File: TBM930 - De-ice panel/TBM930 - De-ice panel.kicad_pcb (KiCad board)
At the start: 2 copper layers, 190.5 x 101.6 mm, 23 parts, among them Q1 BS170, Q2 BS170, Q3 BS170, SW1 SW_SPDT, SW2 SW_SPDT, SW3 SW_SPDT, SW4 SW_SPDT, SW5 SW_SPDT, SW6 SW_SPDT, SW7 SW_SPDT, U1 ArduinoMEGA2560PROEmbed

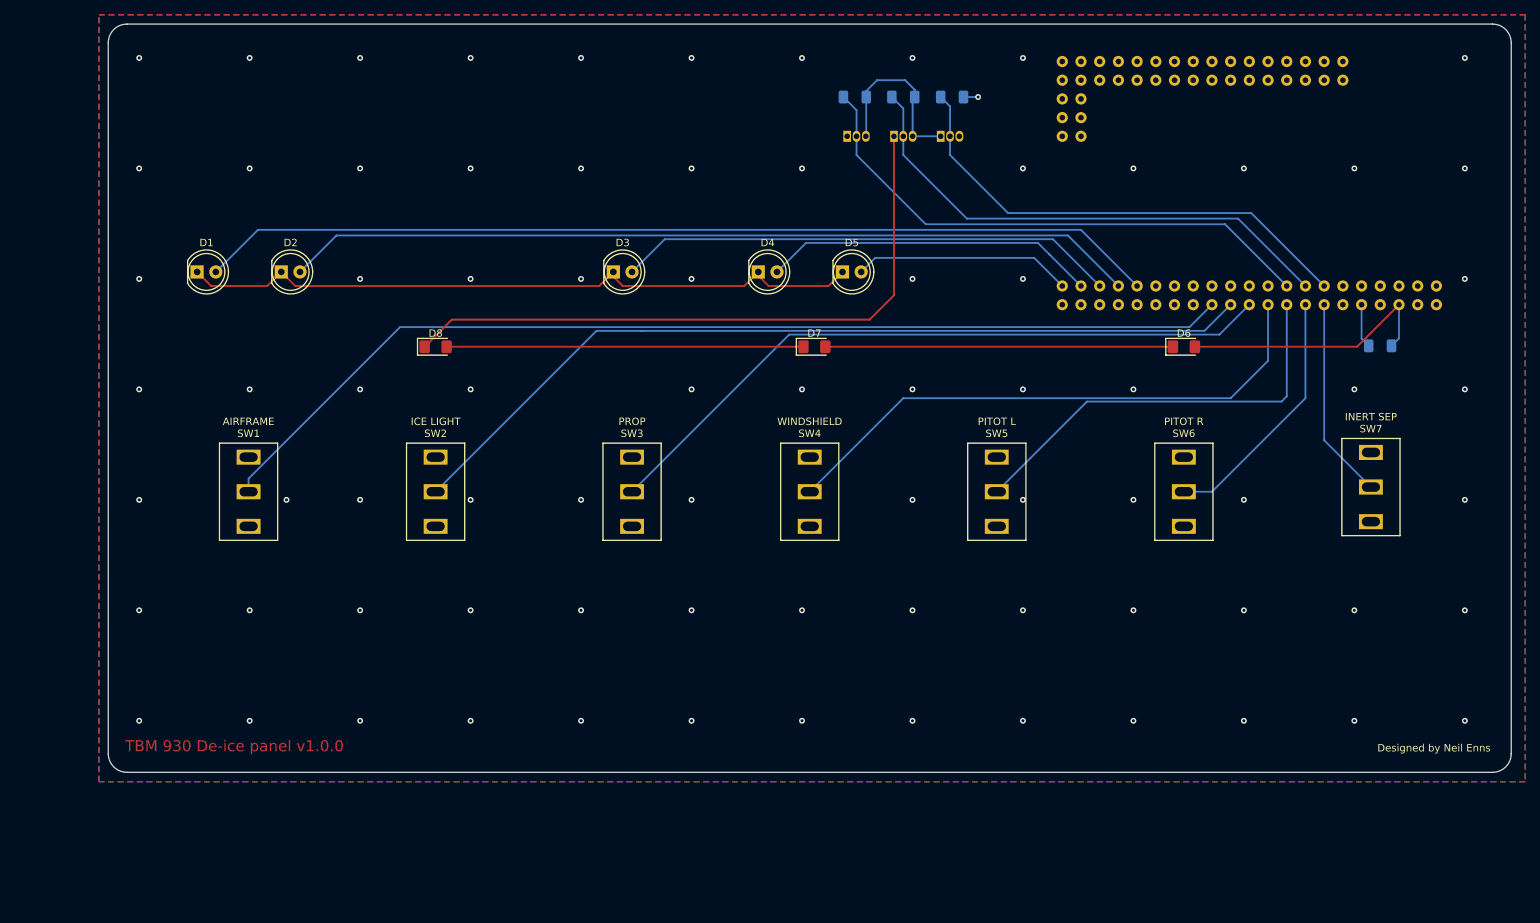
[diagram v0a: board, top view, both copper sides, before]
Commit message: Switch to use the LED driver chip
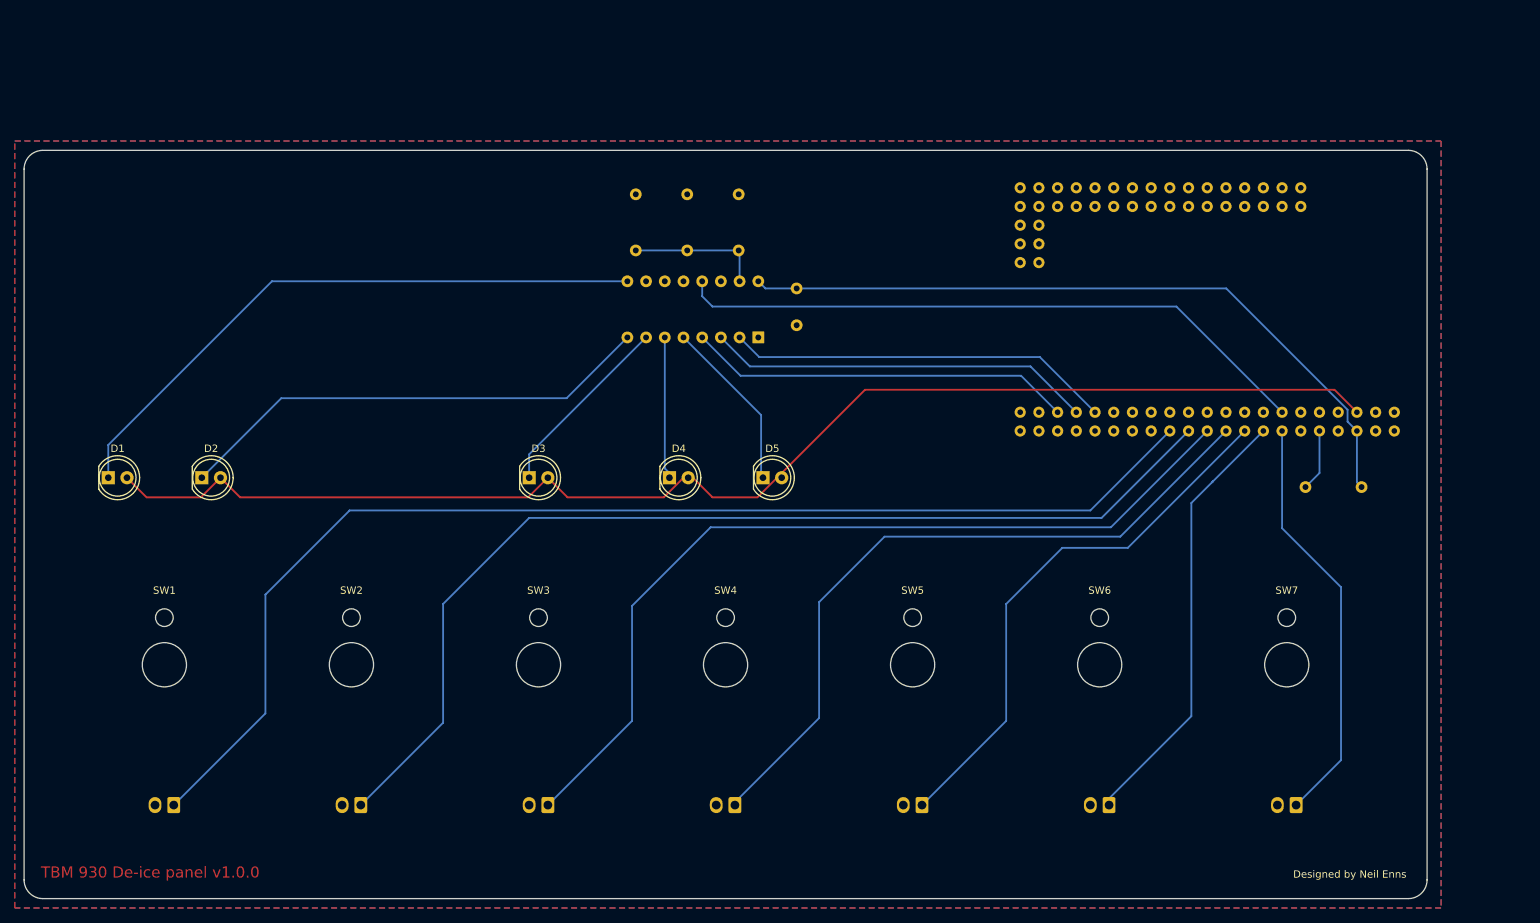
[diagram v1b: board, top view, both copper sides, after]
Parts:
- removed D6, D7, D8: LED, LED_SMD:LED_1206_3216Metric_Pad1.42x1.75mm_HandSolder
- removed Q1, Q2, Q3: BS170, Package_TO_SOT_THT:TO-92_Inline
- added C1: 0.1uF, Capacitor_THT:C_Disc_D5.0mm_W2.5mm_P5.00mm, B.Cu at (144.3, 66.3)
- added J1: SW_AIRFRAME_DE_ICE, Connector_Molex:Molex_KK-254_AE-6410-02A_1x02_P2.54mm_Vertical, B.Cu at (59.7, 131.4)
- added J2: SW_ICE_LIGHT, Connector_Molex:Molex_KK-254_AE-6410-02A_1x02_P2.54mm_Vertical, B.Cu at (85.1, 131.4)
- added J3: SW_PROP_DE_ICE, Connector_Molex:Molex_KK-254_AE-6410-02A_1x02_P2.54mm_Vertical, B.Cu at (110.5, 131.4)
- added J4: SW_WIND_SHIELD, Connector_Molex:Molex_KK-254_AE-6410-02A_1x02_P2.54mm_Vertical, B.Cu at (135.9, 131.4)
- added J5: SW_PITOT_L_HTR, Connector_Molex:Molex_KK-254_AE-6410-02A_1x02_P2.54mm_Vertical, B.Cu at (161.3, 131.4)
- added J6: SW_PITOT_R_HTR, Connector_Molex:Molex_KK-254_AE-6410-02A_1x02_P2.54mm_Vertical, B.Cu at (186.7, 131.4)
- added J7: SW_INERT_SEP, Connector_Molex:Molex_KK-254_AE-6410-02A_1x02_P2.54mm_Vertical, B.Cu at (212.1, 131.4)
- added U2: TLC5916IN, Package_DIP:DIP-16_W7.62mm_Socket, B.Cu at (139.1, 67.9)
- D4: value WINDSHILED 1 -> WINDSHIELD 1
- R1: footprint Resistor_SMD:R_1206_3216Metric_Pad1.30x1.75mm_HandSolder -> Resistor_THT:R_Axial_DIN0207_L6.3mm_D2.5mm_P7.62mm_Horizontal
- R2, R3, R4: value 10k -> R; footprint Resistor_SMD:R_1206_3216Metric_Pad1.30x1.75mm_HandSolder -> Resistor_THT:R_Axial_DIN0207_L6.3mm_D2.5mm_P7.62mm_Horizontal
- SW1, SW2, SW3, SW4, SW5, SW6, SW7: value SW_SPDT -> Mini toggle - SPDT; footprint Switches:MiniToggleSPDTterminalmount -> Switches:MiniToggleSPDT screw mount
- moved R4 44.9 mm to (122.4, 48.5), turned to 270 degrees
- moved R3 32.2 mm to (129.4, 48.5), turned to 270 degrees
- moved D1 30.4 mm to (50.8, 87.0)
- moved D4 30.4 mm to (127.0, 87.0)
- moved D3 30.2 mm to (108.0, 87.0)
- moved D5 30.0 mm to (139.7, 87.0)
- moved D2 30.0 mm to (63.5, 87.0)
- moved SW3 26.7 mm to (109.2, 112.4)
- moved SW7 26.7 mm to (210.8, 112.4)
- moved SW2 26.1 mm to (83.8, 112.4)
- moved SW4 26.1 mm to (134.6, 112.4)
- moved SW6 26.1 mm to (185.4, 112.4)
- moved SW1 26.1 mm to (58.4, 112.4)
- moved SW5 26.1 mm to (160.0, 112.4)
- moved R2 20.6 mm to (136.4, 48.5), turned to 270 degrees
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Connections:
- D1 pad 1: ANC_GND -> AIRFRAME_1
- D1 pad 2: AIRFRAME_1_LED -> +5V_LED
- D2 pad 1: ANC_GND -> AIRFRAME_2
- D2 pad 2: AIRFRAME_2_LED -> +5V_LED
- D3 pad 1: ANC_GND -> PROP
- D3 pad 2: PROP_LED -> +5V_LED
- D4 pad 1: ANC_GND -> WINDSHIELD_1
- D4 pad 2: WINDSHIELD_1_LED -> +5V_LED
- D5 pad 1: ANC_GND -> WINDSHIELD_2
- D5 pad 2: WINDSHIELD_2_LED -> +5V_LED
- R2 pad 1: ANNUNCIATOR_BRIGHTNESS -> GND
- R2 pad 2: LED_MASTER_GND -> CURRENT_LIMITER
- R3 pad 1: BACKLIGHT_BRIGHTNESS -> GND
- R3 pad 2: LED_MASTER_GND -> CURRENT_LIMITER
- R4 pad 1: MASTER_POWER -> GND
- R4 pad 2: GND -> CURRENT_LIMITER
- U1 pad 14: MASTER_POWER -> ANNUNCIATOR_BRIGHTNESS
- U1 pad 16: BACKLIGHT_BRIGHTNESS -> Net-(U1-Pad16)
- U1 pad 18: ANNUNCIATOR_BRIGHTNESS -> Net-(U1-Pad18)
- U1 pad 34: AIRFRAME_1_LED -> ANNUNCIATOR_DATA
- U1 pad 36: AIRFRAME_2_LED -> ANNUNCIATOR_CLOCK
- U1 pad 38: PROP_LED -> ANNUNCIATOR_LATCH
- U1 pad 40: WINDSHIELD_1_LED -> Net-(U1-Pad40)
- U1 pad 42: WINDSHIELD_2_LED -> Net-(U1-Pad42)
- U1 pad 6: Net-(U1-Pad6) -> +5V_LED
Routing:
- net +5V_LED: track 0.00 -> 182.6 mm
- net AIRFRAME_1_LED: track 130.6 -> 0.00 mm
- net AIRFRAME_2_LED: track 116.0 -> 0.00 mm
- net ANC_GND: track 94.7 -> 0.00 mm
- net BACKLIGHT_GND: track 88.2 -> 0.00 mm
- net AIRFRAME_1: track 0.00 -> 84.1 mm
- net BACKLIGHT_BRIGHTNESS: track 70.5 -> 0.00 mm
- net PROP_LED: track 68.0 -> 0.00 mm
- net MASTER_POWER: track 66.6 -> 0.00 mm
- net AIRFRAME_2: track 0.00 -> 65.7 mm
- net +5V: track 36.1 -> 98.5 mm
- net ANNUNCIATOR_LATCH: track 0.00 -> 52.5 mm
- net ANNUNCIATOR_DATA: track 0.00 -> 52.5 mm
- net ANNUNCIATOR_CLOCK: track 0.00 -> 52.5 mm
- net Net-(D7-Pad1): track 48.7 -> 0.00 mm
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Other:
- board text added: "SW_AIRFRAME_DE_ICE"
- board text added: "SW_ICE_LIGHT"
- board text added: "SW_INERT_SEP"
- board text added: "SW_PITOT_L_HTR"
- board text added: "SW_PITOT_R_HTR"
- board text added: "SW_PROP_DE_ICE"
- board text added: "SW_WIND_SHIELD"
- board text removed: "AIRFRAME"
- board text removed: "ICE LIGHT"
- board text removed: "INERT SEP"
- board text removed: "PITOT L"
- board text removed: "PITOT R"
- board text removed: "PROP"
- board text removed: "WINDSHIELD"

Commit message: Create global library for footprints and symbols
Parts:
- SW1, SW2, SW3, SW4, SW5, SW6, SW7: footprint Switches:MiniToggleSPDT screw mount -> Global MobiFlight panel parts:MiniToggleSPDT_screw_mount
- U1: footprint Ardino:MEGA2560PROEmbed -> Global MobiFlight panel parts:MEGA2560PROEmbed

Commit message: Massive de-ice panel update
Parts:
- removed R4: R, Resistor_THT:R_Axial_DIN0207_L6.3mm_D2.5mm_P7.62mm_Horizontal
- added C2: 0.1uF, Capacitor_THT:C_Disc_D5.0mm_W2.5mm_P5.00mm, B.Cu at (99.1, 59.7)
- added D10: LED, LED_SMD:LED_1206_3216Metric_Pad1.42x1.75mm_HandSolder, F.Cu at (160.0, 78.1)
- added D11: LED, LED_SMD:LED_1206_3216Metric_Pad1.42x1.75mm_HandSolder, F.Cu at (185.5, 78.1)
- added D12: LED, LED_SMD:LED_1206_3216Metric_Pad1.42x1.75mm_HandSolder, F.Cu at (210.8, 78.1)
- added D13: LED, LED_SMD:LED_1206_3216Metric_Pad1.42x1.75mm_HandSolder, F.Cu at (110.3, 112.4)
- added D14: LED, LED_SMD:LED_1206_3216Metric_Pad1.42x1.75mm_HandSolder, F.Cu at (226.1, 67.9)
- added D15: LED, LED_SMD:LED_1206_3216Metric_Pad1.42x1.75mm_HandSolder, F.Cu at (226.1, 118.7)
- added D15: LED, LED_SMD:LED_1206_3216Metric_Pad1.42x1.75mm_HandSolder, F.Cu at (182.2, 140.3)
- added D16: LED, LED_SMD:LED_1206_3216Metric_Pad1.42x1.75mm_HandSolder, F.Cu at (134.6, 140.3)
- added D17: LED, LED_SMD:LED_1206_3216Metric_Pad1.42x1.75mm_HandSolder, F.Cu at (87.0, 140.3)
- added D18: LED, LED_SMD:LED_1206_3216Metric_Pad1.42x1.75mm_HandSolder, F.Cu at (43.2, 118.7)
- added D19: LED, LED_SMD:LED_1206_3216Metric_Pad1.42x1.75mm_HandSolder, F.Cu at (43.2, 67.9)
- added D20: LED, LED_SMD:LED_1206_3216Metric_Pad1.42x1.75mm_HandSolder, F.Cu at (134.6, 45.7)
- added D21: LED, LED_SMD:LED_1206_3216Metric_Pad1.42x1.75mm_HandSolder, F.Cu at (182.2, 45.7)
- added D22: LED, LED_SMD:LED_1206_3216Metric_Pad1.42x1.75mm_HandSolder, F.Cu at (87.0, 45.7)
- added D6: LED, LED_SMD:LED_1206_3216Metric_Pad1.42x1.75mm_HandSolder, F.Cu at (58.4, 78.1)
- added D7: LED, LED_SMD:LED_1206_3216Metric_Pad1.42x1.75mm_HandSolder, F.Cu at (83.8, 78.1)
- added D8: LED, LED_SMD:LED_1206_3216Metric_Pad1.42x1.75mm_HandSolder, F.Cu at (109.2, 78.1)
- added D9: LED, LED_SMD:LED_1206_3216Metric_Pad1.42x1.75mm_HandSolder, F.Cu at (134.6, 78.1)
- added J8: Barrel_Jack, Global MobiFlight panel parts:BarrelJack_Horizontal, F.Cu at (220.0, 55.6)
- added SW8: Mini toggle - SPDT, Global MobiFlight panel parts:MiniToggleSPDT_screw_mount, F.Cu at (210.8, 93.3)
- added U3: TLC5917IN, Package_DIP:DIP-16_W7.62mm, B.Cu at (92.7, 61.6)
- R1: moved to F.Cu
- R2, R3: value R -> 1k; moved to F.Cu
- SW1: value Mini toggle - SPDT -> SW_Push; footprint Global MobiFlight panel parts:MiniToggleSPDT_screw_mount -> Button_Switch_THT:SW_PUSH_6mm_H9.5mm
- U2: value TLC5916IN -> TLC5917IN; footprint Package_DIP:DIP-16_W7.62mm_Socket -> Package_DIP:DIP-16_W7.62mm
- moved J7 113.4 mm to (98.8, 126.4)
- moved J6 102.0 mm to (84.8, 126.4)
- moved J5 90.8 mm to (70.6, 126.4)
- moved J4 79.4 mm to (56.6, 126.4)
- moved U1 59.6 mm to (197.6, 122.4), turned to 270 degrees
- moved R1 52.8 mm to (169.2, 98.3), turned to 0 degrees
- moved R3 47.1 mm to (85.7, 66.0), turned to 0 degrees
- moved C1 36.0 mm to (179.7, 59.7)
- moved U2 35.0 mm to (173.4, 61.0)
- moved R2 34.4 mm to (166.4, 65.4), turned to 0 degrees
- moved SW1 34.3 mm to (92.7, 110.5)
- moved J3 32.2 mm to (84.6, 112.4)
- moved SW3 31.8 mm to (83.8, 93.3)
- moved SW4 31.8 mm to (109.2, 93.3)
- moved SW5 31.8 mm to (134.6, 93.3)
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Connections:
- net ANNUNCIATOR_CLOCK renamed LED_CLOCK
- net ANNUNCIATOR_DATA renamed LED_DATA
- net ANNUNCIATOR_LATCH renamed LED_LATCH
- J4 pad 2: Net-(J4-Pad2) -> GND
- R2 pad 1: GND -> Net-(R2-Pad1)
- R2 pad 2: CURRENT_LIMITER -> GND
- R3 pad 1: GND -> Net-(R3-Pad1)
- R3 pad 2: CURRENT_LIMITER -> GND
- U1 pad 16: Net-(U1-Pad16) -> BACKLIGHT_BRIGHTNESS
- U1 pad 27: Net-(U1-Pad27) -> LTS_TEST
- U2 pad 15: CURRENT_LIMITER -> Net-(R2-Pad1)
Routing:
- net +5V_LED: track 182.6 -> 0.00 mm
- net AIRFRAME_DE_ICE: track 165.7 -> 0.00 mm
- net ICE_LIGHT: track 142.9 -> 0.00 mm
- net PROP_DE_ICE: track 119.7 -> 0.00 mm
- net +5V: track 98.5 -> 0.00 mm
- net WIND_SHIELD: track 97.2 -> 0.00 mm
- net ANNUNCIATOR_BRIGHTNESS: track 87.3 -> 0.00 mm
- net AIRFRAME_1: track 84.1 -> 0.00 mm
- net PITOT_L_HTR: track 74.2 -> 0.00 mm
- net AIRFRAME_2: track 65.7 -> 0.00 mm
- net PITOT_R_HTR: track 59.7 -> 0.00 mm
- net INERT_SEP: track 56.6 -> 0.00 mm
- net LED_LATCH: track 52.5 -> 0.00 mm
- net LED_DATA: track 52.5 -> 0.00 mm
- net LED_CLOCK: track 52.5 -> 0.00 mm
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
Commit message: Routed!
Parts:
- removed the D15 at (226.1, 118.7)
- removed the D15 at (182.2, 140.3)
- added D15: LED, LED_SMD:LED_1206_3216Metric_Pad1.42x1.75mm_HandSolder, F.Cu at (226.1, 67.9)
- added D23: LED, LED_SMD:LED_1206_3216Metric_Pad1.42x1.75mm_HandSolder, F.Cu at (182.2, 46.4)
- added D24: LED, LED_SMD:LED_1206_3216Metric_Pad1.42x1.75mm_HandSolder, F.Cu at (134.6, 46.4)
- J8: moved to B.Cu
- moved D21 140.8 mm to (43.2, 67.9), turned to 90 degrees
- moved D14 125.0 mm to (109.2, 112.4), turned to 0 degrees
- moved D20 117.0 mm to (43.2, 118.7), turned to 90 degrees
- moved D13 106.2 mm to (210.8, 78.1)
- moved D17 95.2 mm to (182.2, 140.3)
- moved D16 94.0 mm to (226.1, 118.7), turned to 90 degrees
- moved D18 94.0 mm to (134.6, 140.3), turned to 0 degrees
- moved D19 84.6 mm to (87.0, 140.3), turned to 0 degrees
- moved D11 25.4 mm to (160.0, 78.1)
- moved D10 25.4 mm to (134.6, 78.1)
- moved D9 25.4 mm to (109.2, 78.1)
- moved D7 25.4 mm to (58.4, 78.1)
- moved D12 25.4 mm to (185.4, 78.1)
- moved D8 25.4 mm to (83.8, 78.1)
- moved D6 18.9 mm to (47.6, 93.6), turned to 90 degrees
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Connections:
- D13 pad 1: BACKLIGHT3 -> Net-(D13-Pad1)
- D14 pad 1: Net-(D14-Pad1) -> BACKLIGHT3
- D14 pad 2: +12V_LED -> Net-(D13-Pad1)
- D16 pad 1: BACKLIGHT4 -> Net-(D16-Pad1)
- D17 pad 1: Net-(D17-Pad1) -> BACKLIGHT4
- D17 pad 2: +12V_LED -> Net-(D16-Pad1)
- D18 pad 2: Net-(D17-Pad1) -> +12V_LED
- D19 pad 1: BACKLIGHT5 -> Net-(D19-Pad1)
- D20 pad 1: Net-(D20-Pad1) -> BACKLIGHT5
- D20 pad 2: +12V_LED -> Net-(D19-Pad1)
- D21 pad 2: Net-(D20-Pad1) -> +12V_LED
- U1 pad 13: INERT_SEP -> Net-(U1-Pad13)
- U1 pad 14: ANNUNCIATOR_BRIGHTNESS -> Net-(U1-Pad14)
- U1 pad 15: PITOT_R_HTR -> ANNUNCIATOR_BRIGHTNESS
- U1 pad 16: BACKLIGHT_BRIGHTNESS -> Net-(U1-Pad16)
- U1 pad 17: PITOT_L_HTR -> BACKLIGHT_BRIGHTNESS
- U1 pad 18: Net-(U1-Pad18) -> AIRFRAME_DE_ICE
- U1 pad 19: WIND_SHIELD -> Net-(U1-Pad19)
- U1 pad 20: Net-(U1-Pad20) -> ICE_LIGHT
- U1 pad 21: PROP_DE_ICE -> Net-(U1-Pad21)
- U1 pad 22: Net-(U1-Pad22) -> PROP_DE_ICE
- U1 pad 23: ICE_LIGHT -> Net-(U1-Pad23)
- U1 pad 24: Net-(U1-Pad24) -> LTS_TEST
- U1 pad 25: AIRFRAME_DE_ICE -> Net-(U1-Pad25)
- U1 pad 26: Net-(U1-Pad26) -> WIND_SHIELD
- U1 pad 27: LTS_TEST -> Net-(U1-Pad27)
- U1 pad 28: Net-(U1-Pad28) -> PITOT_L_HTR
- U1 pad 30: Net-(U1-Pad30) -> PITOT_R_HTR
- U1 pad 32: Net-(U1-Pad32) -> INERT_SEP
- U1 pad 33: Net-(U1-Pad33) -> LED_DATA
- U1 pad 34: LED_DATA -> Net-(U1-Pad34)
- U1 pad 35: Net-(U1-Pad35) -> LED_CLOCK
- U1 pad 36: LED_CLOCK -> Net-(U1-Pad36)
- U1 pad 37: Net-(U1-Pad37) -> LED_LATCH
- U1 pad 38: LED_LATCH -> Net-(U1-Pad38)
- U3 pad 11: Net-(U3-Pad11) -> BACKLIGHT7
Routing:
- net +12V_LED: track 0.00 -> 314.9 mm, vias 0 -> 2
- net LED_LATCH: track 0.00 -> 155.6 mm
- net WIND_SHIELD: track 0.00 -> 154.0 mm
- net LED_CLOCK: track 0.00 -> 150.6 mm
- net +5V: track 0.00 -> 148.5 mm
- net +5V_LED: track 0.00 -> 147.5 mm
- net BACKLIGHT4: track 0.00 -> 146.7 mm, vias 0 -> 1
- net PITOT_L_HTR: track 0.00 -> 142.6 mm
- net AIRFRAME_DE_ICE: track 0.00 -> 139.0 mm
- net BACKLIGHT_BRIGHTNESS: track 0.00 -> 132.0 mm
- net PITOT_R_HTR: track 0.00 -> 130.9 mm
- net Net-(D13-Pad1): track 0.00 -> 126.6 mm
- net ICE_LIGHT: track 0.00 -> 126.6 mm
- net INERT_SEP: track 0.00 -> 119.4 mm
- net PROP_DE_ICE: track 0.00 -> 115.2 mm
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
